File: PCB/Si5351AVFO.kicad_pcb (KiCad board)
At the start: 4 copper layers, 100 x 65 mm, 127 parts, among them J1 USB_C_Receptacle, J2 SMA CLK0, J3 SMA CLK1, J4 SMA CLK2, J5 UPDI, SW1 EC11E18244A5, SW2 BAND, SW3 STEP, SW4 MENU, U1 LP2985-3.3, U2 Si5351A-B-GT, U3 CP2102N-A02-GQFN24, U4 ATtiny3226-SU, U5 LP2985-3.3, X1 25MHz TCXO

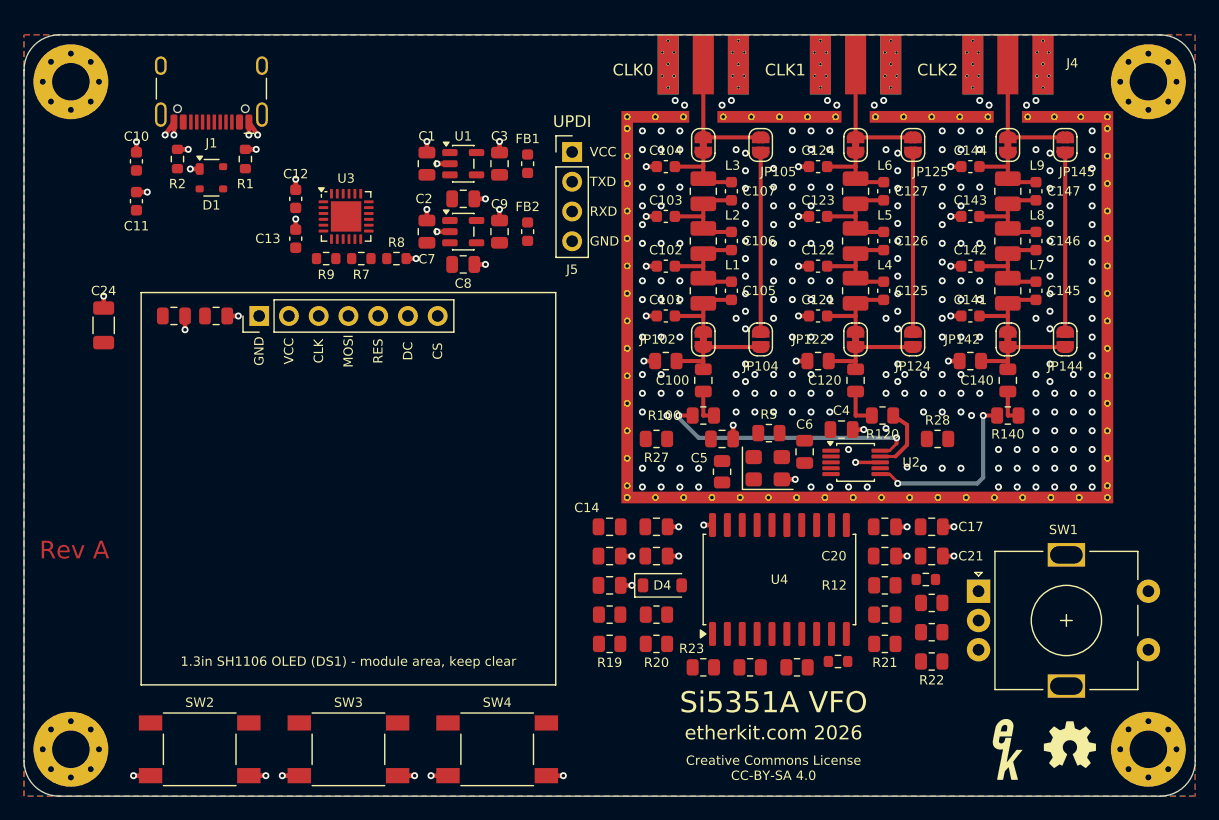
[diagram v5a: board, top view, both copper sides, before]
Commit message: PCB: re-place MCU area (U4 rot 0, passives by pin side); freerouted power+digital (WIP, 26 unconnected); Alps EC11E18244A5 model for SW1; regen board STEP
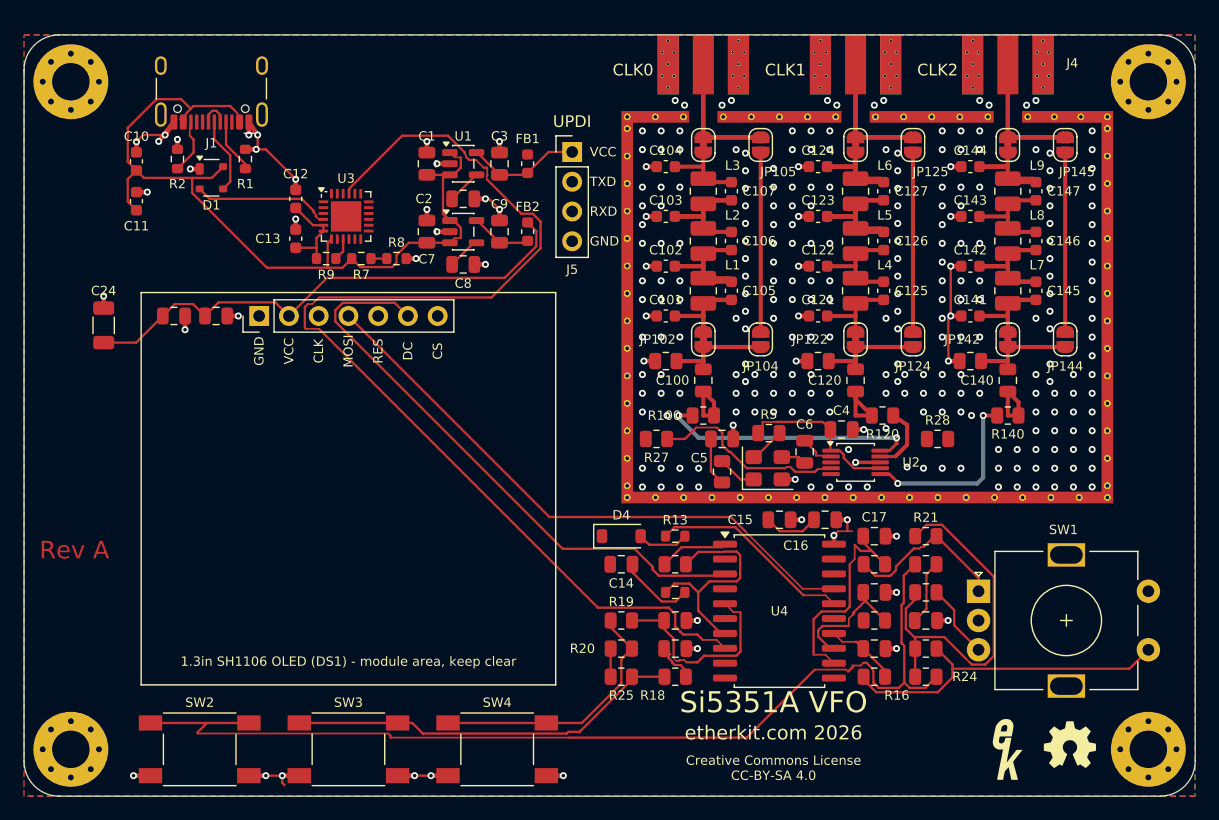
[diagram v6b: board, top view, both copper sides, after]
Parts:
- moved C21 23.3 mm to (155.6, 152.4)
- moved C18 22.8 mm to (172.6, 147.6)
- moved R15 22.6 mm to (172.6, 150.0)
- moved R18 22.2 mm to (155.6, 154.8)
- moved R13 21.7 mm to (155.6, 142.8)
- moved C19 20.2 mm to (172.6, 152.4)
- moved R16 19.3 mm to (172.6, 154.8)
- moved R23 19.1 mm to (177.0, 152.4)
- moved R12 18.0 mm to (155.6, 145.2)
- moved R29 15.1 mm to (155.6, 147.6)
- moved R24 15.0 mm to (177.0, 154.8)
- moved R25 15.0 mm to (151.0, 154.8)
- moved C15 10.5 mm to (164.5, 141.4)
- moved R21 9.84 mm to (177.0, 142.8)
- moved C20 6.52 mm to (177.0, 150.0)
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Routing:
- net MCU_RX: track 0.00 -> 96.6 mm
- net /MCU and UI/BTN_BAND_SW: track 0.00 -> 88.8 mm
- net +5V: track 0.00 -> 72.3 mm
- net +3V3D: track 0.00 -> 54.4 mm
- net /MCU and UI/OLED_MOSI: track 0.00 -> 51.1 mm
- net /MCU and UI/OLED_DC: track 0.00 -> 50.3 mm
- net +3V3_OLED: track 0.00 -> 44.5 mm
- net /MCU and UI/BTN_STEP_SW: track 0.00 -> 33.7 mm
- net /MCU and UI/ENC_SW_SW: track 0.00 -> 29.2 mm
- net GND: track 59.2 -> 84.7 mm
- net /MCU and UI/BTN_MENU_SW: track 0.00 -> 22.7 mm
- net Net-(U4-PB4): track 0.00 -> 19.3 mm
- net /MCU and UI/ENC_A: track 0.00 -> 18.9 mm
- net /MCU and UI/BTN_MENU: track 0.00 -> 17.6 mm
- net /MCU and UI/UPDI_PA0: track 0.00 -> 17.4 mm
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
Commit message: PCB: route power nets (USB VBUS, LDOs, +5V/+3V3 rails) via freerouting; add tools/pcbgen build scripts; U3 EP vias; OLED-area F.Cu track keepout
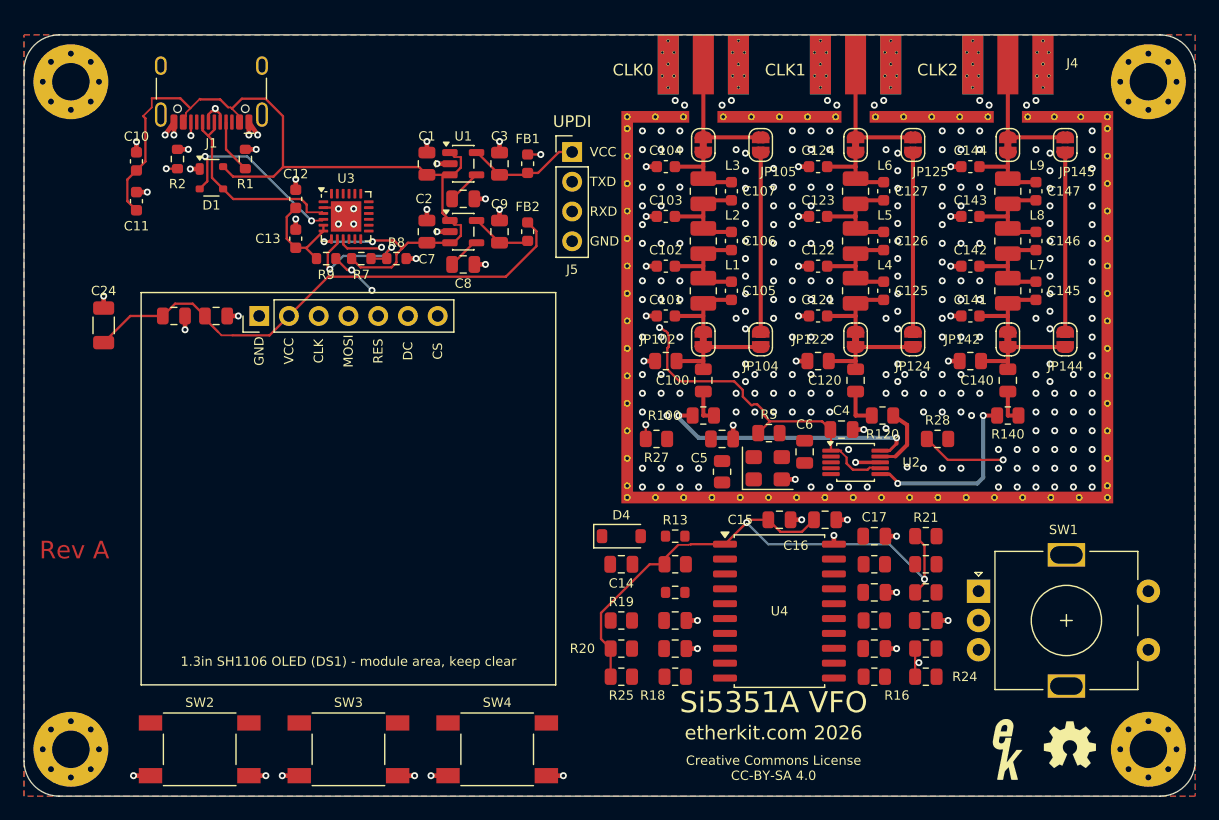
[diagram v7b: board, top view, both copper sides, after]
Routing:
- net MCU_RX: track 96.6 -> 0.00 mm
- net /MCU and UI/BTN_BAND_SW: track 88.8 -> 0.00 mm
- net +3V3D: track 54.4 -> 138.3 mm, vias 0 -> 5
- net /MCU and UI/OLED_MOSI: track 51.1 -> 0.00 mm
- net /MCU and UI/OLED_DC: track 50.3 -> 0.00 mm
- net +3V3_CLK: track 14.0 -> 55.2 mm, vias 0 -> 2
- net /MCU and UI/BTN_STEP_SW: track 33.7 -> 0.00 mm
- net /MCU and UI/ENC_SW_SW: track 29.2 -> 0.00 mm
- net GND: track 84.7 -> 60.7 mm, vias 300 -> 304
- net /MCU and UI/BTN_MENU_SW: track 22.7 -> 0.00 mm
- net Net-(U4-PB4): track 19.3 -> 0.00 mm
- net /MCU and UI/ENC_A: track 18.9 -> 0.00 mm
- net /MCU and UI/BTN_MENU: track 17.6 -> 0.00 mm
- net /MCU and UI/UPDI_PA0: track 17.4 -> 0.00 mm
- net I2C_SCL: track 16.8 -> 0.00 mm
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
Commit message: PCB: route digital nets (CP2102N, ATtiny, OLED SPI, buttons/encoder, I2C, UPDI); DRC 0 unconnected
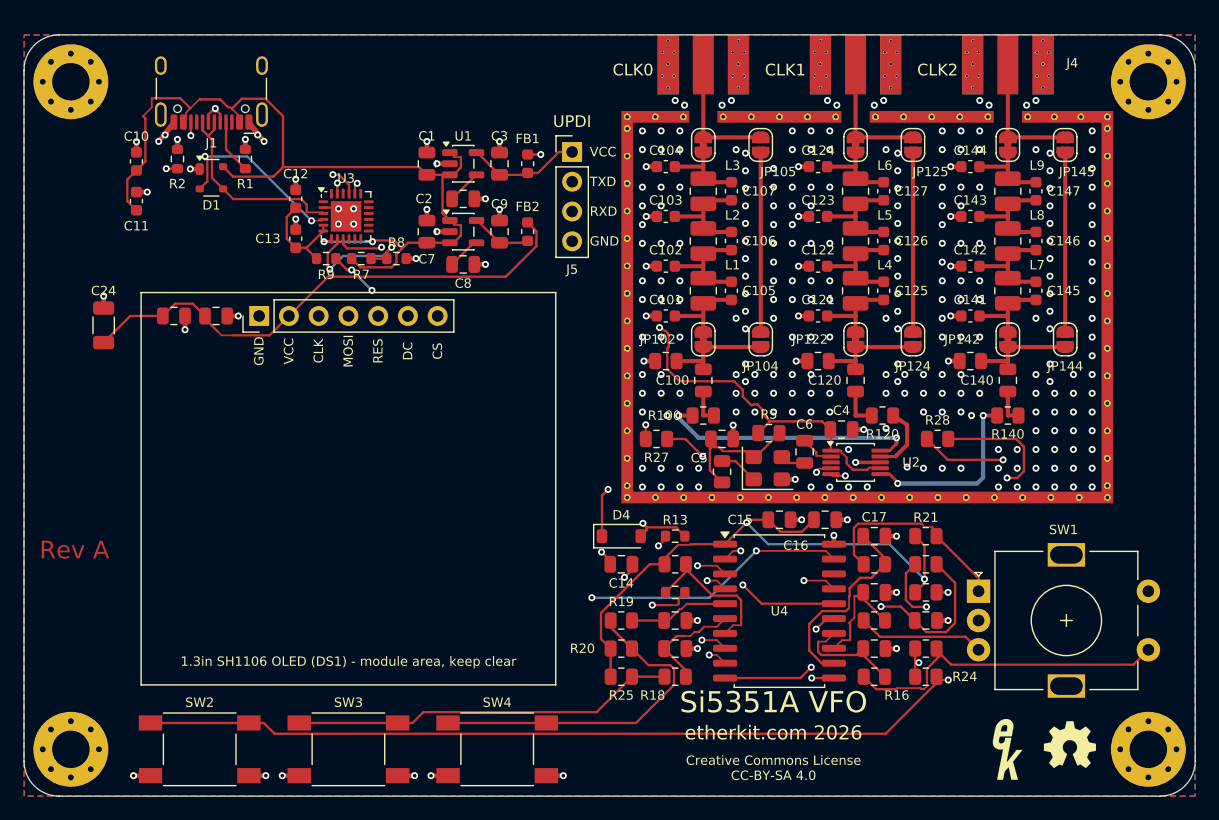
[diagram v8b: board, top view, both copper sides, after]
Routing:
- net /MCU and UI/BTN_BAND_SW: track 0.00 -> 83.3 mm, vias 0 -> 2
- net MCU_RX: track 0.00 -> 63.4 mm, vias 0 -> 2
- net MCU_TX: track 0.00 -> 59.8 mm, vias 0 -> 2
- net /MCU and UI/OLED_SCK: track 0.00 -> 56.3 mm, vias 0 -> 2
- net I2C_SDA: track 0.00 -> 55.4 mm, vias 0 -> 3
- net /MCU and UI/OLED_MOSI: track 0.00 -> 51.9 mm, vias 0 -> 1
- net DTR: track 0.00 -> 45.6 mm, vias 0 -> 2
- net /MCU and UI/OLED_RES: track 0.00 -> 39.4 mm, vias 0 -> 1
- net /MCU and UI/OLED_CS: track 0.00 -> 36.5 mm, vias 0 -> 1
- net /MCU and UI/OLED_DC: track 0.00 -> 36.2 mm, vias 0 -> 1
- net I2C_SCL: track 0.00 -> 35.7 mm, vias 0 -> 3
- net Net-(D4-A): track 0.00 -> 35.1 mm, vias 0 -> 1
- net /MCU and UI/UPDI_TXD: track 0.00 -> 33.0 mm, vias 0 -> 1
- net /MCU and UI/BTN_STEP_SW: track 0.00 -> 32.8 mm
- net /MCU and UI/BTN_MENU_SW: track 0.00 -> 29.5 mm
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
